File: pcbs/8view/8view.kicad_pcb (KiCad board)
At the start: 4 copper layers, 23.6 x 35.6 mm, 40 parts, among them J1 Conn_01x10_Female, J2 Conn_01x10_Female, J3 Conn_01x06_Female, J4 Conn_01x06_Female, U1 ATtiny828-A, U2 HDSP-A151, U3 HDSP-A151

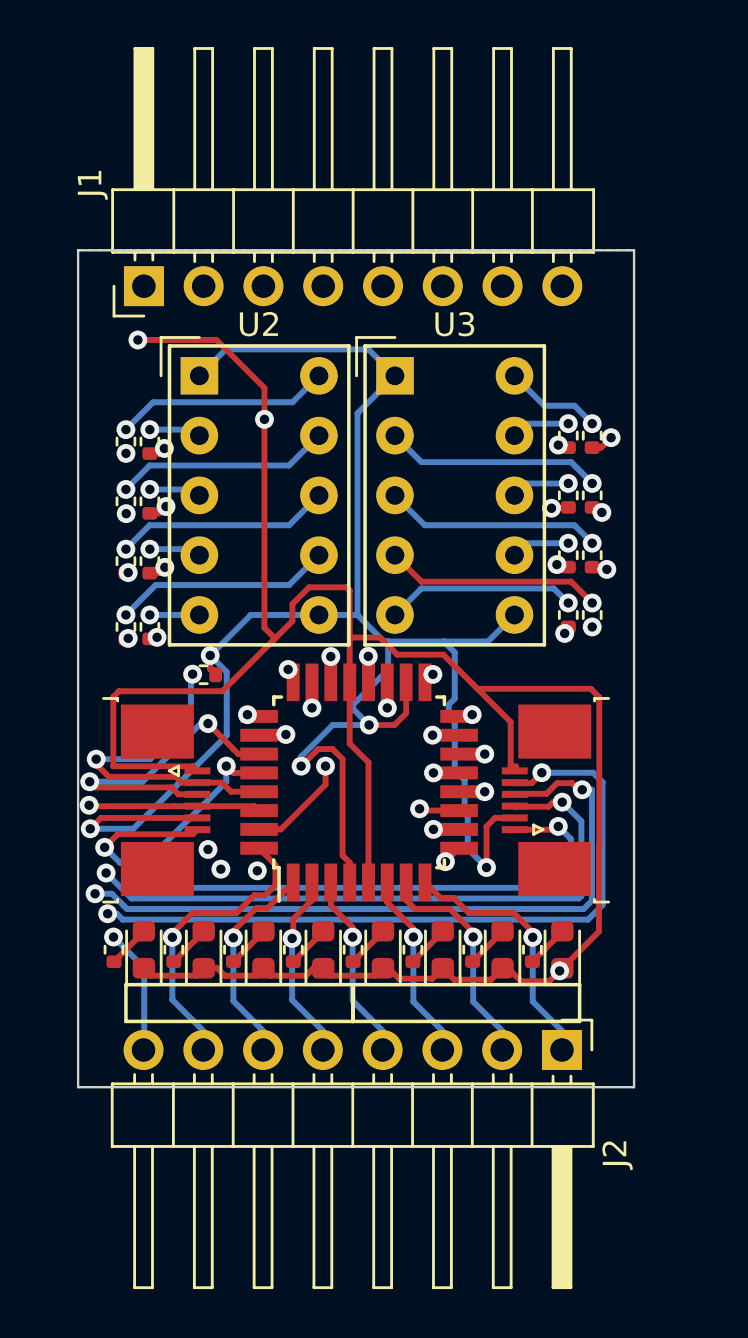
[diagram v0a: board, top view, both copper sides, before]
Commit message: v1 8view borads
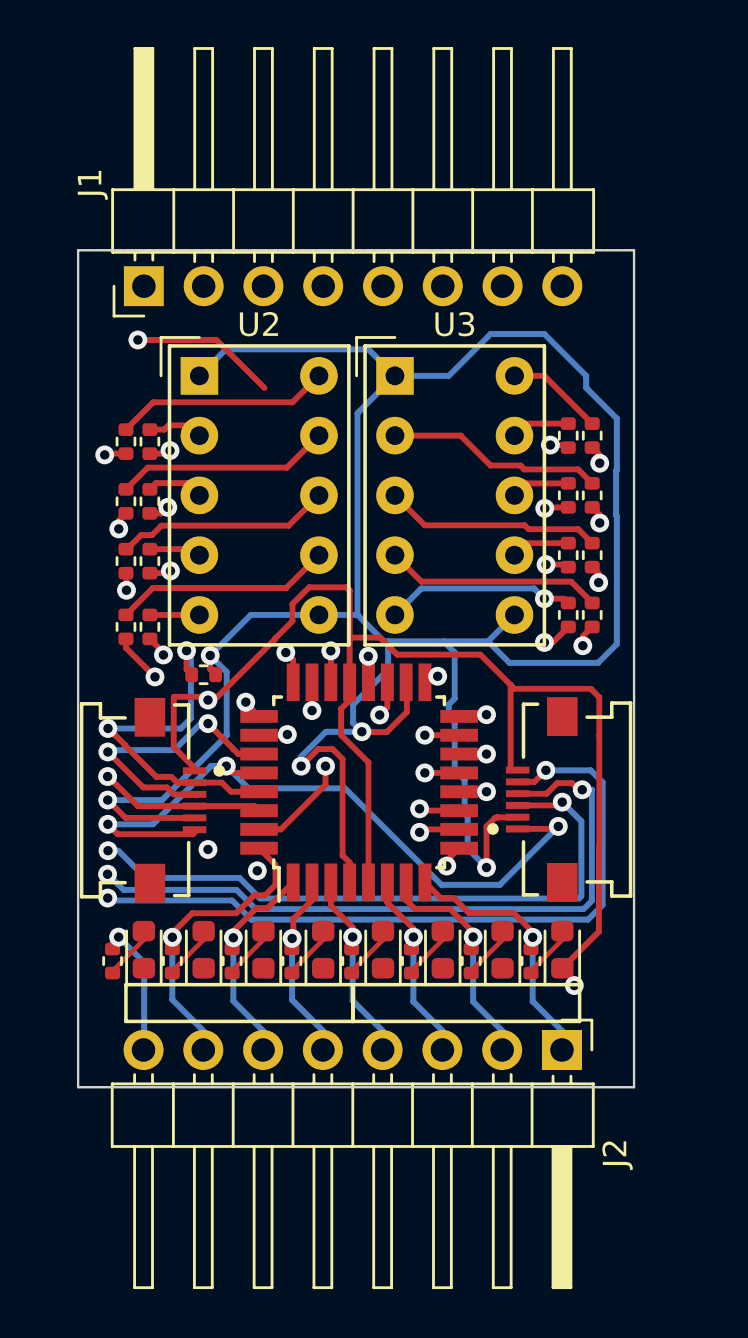
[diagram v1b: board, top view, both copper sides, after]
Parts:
- J3, J4: footprint Connector_FFC-FPC:TE_0-1734839-6_1x06-1MP_P0.5mm_Horizontal -> ffc:Molex-54550-0671-Manufacturer_Recommended
- moved R1 0.49 mm to (137.1, 147.0)
- moved R2 0.49 mm to (139.6, 147.0)
- moved R3 0.49 mm to (142.2, 147.0)
- moved R4 0.49 mm to (144.7, 147.0)
- moved R5 0.49 mm to (147.3, 147.0)
- moved R6 0.49 mm to (149.8, 147.0)
- moved R7 0.49 mm to (152.3, 147.0)
- moved R8 0.49 mm to (154.9, 147.0)
- moved J3 0.28 mm to (155.3, 140.2)
- moved J4 0.28 mm to (139.6, 140.2)
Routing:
- net +5V: track 84.1 -> 110.3 mm
- net GND: track 96.8 -> 89.8 mm
- net /ISP_MISO: track 37.2 -> 30.6 mm
- net /ISP_RST: track 53.1 -> 56.2 mm
- net /D1_I5: track 28.2 -> 26.5 mm
- net /D1_I3: track 24.6 -> 23.3 mm
- net /ISP_SCK: track 38.3 -> 39.5 mm
- net /D1_I7: track 32.4 -> 31.3 mm
- net /D2_I8: track 18.6 -> 19.6 mm
- net /ISP_MOSI: track 50.0 -> 49.1 mm
- net /in2: track 47.8 -> 48.5 mm
- net Net-(D1-Pad2): track 1.82 -> 2.58 mm
- net /in3: track 44.4 -> 45.0 mm
- net /D2_I1: track 33.0 -> 33.6 mm
- net /D2_I7: track 13.2 -> 12.7 mm
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
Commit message: 8view: 10pin skirt, 1.5k leds
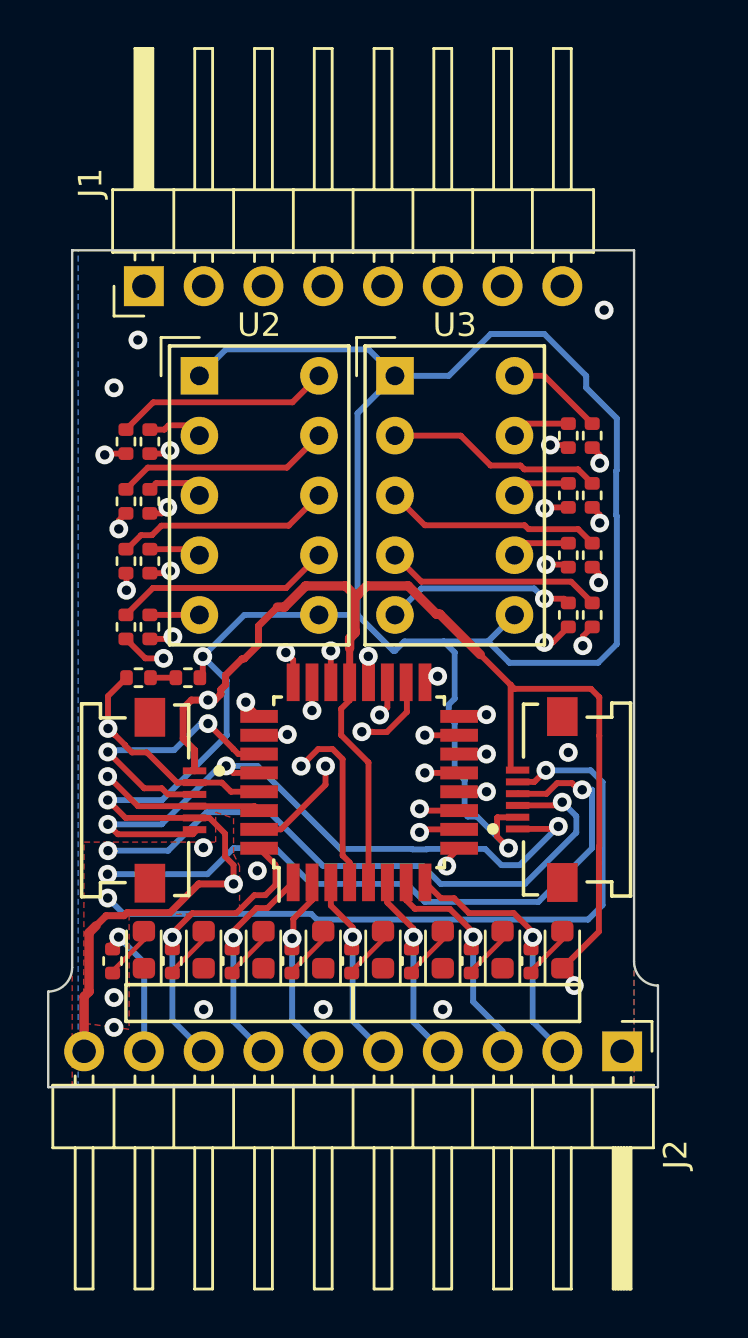
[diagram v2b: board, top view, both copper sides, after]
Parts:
- added R10: 1k5, Resistor_SMD:R_0402_1005Metric, F.Cu at (138.2, 135.0)
- J2: footprint Connector_PinHeader_2.54mm:PinHeader_1x08_P2.54mm_Horizontal -> Connector_PinHeader_2.54mm:PinHeader_1x10_P2.54mm_Horizontal
- R1, R2, R3, R4, R5, R6, R7, R8, R9: value 1000 -> 1k5
- R11: renamed from R10; value 1000 -> 1k
- R12: renamed from R11; value 1000 -> 1k
- R13: renamed from R12; value 1000 -> 1k
- R14: renamed from R13; value 1000 -> 1k
- R15: renamed from R14; value 1000 -> 1k
- R16: renamed from R15; value 1000 -> 1k
- R17: renamed from R16; value 1000 -> 1k
- R18: renamed from R17; value 1000 -> 1k
- R19: renamed from R18; value 1000 -> 1k
- R20: renamed from R19; value 1000 -> 1k
- R21: renamed from R20; value 1000 -> 1k
- R22: renamed from R21; value 1000 -> 1k
- R23: renamed from R22; value 1000 -> 1k
- R24: renamed from R23; value 1000 -> 1k
- R25: renamed from R24; value 1000 -> 1k
- R26: renamed from R25; value 1000 -> 1k
- moved J2 2.56 mm to (158.8, 150.9)
- moved R9 0.68 mm to (140.3, 135.0)
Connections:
- J2 pad 1: /in7 -> GND
- J2 pad 2: /in6 -> /in7
- J2 pad 3: /in5 -> /in6
- J2 pad 4: /in4 -> /in5
- J2 pad 5: /in3 -> /in4
- J2 pad 6: /in2 -> /in3
- J2 pad 7: /in1 -> /in2
- J2 pad 8: /in0 -> /in1
- R9 pad 2: /ISP_RST -> Net-(R9-Pad2)
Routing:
- net GND: track 89.8 -> 76.4 mm, vias 3 -> 7
- net /in0: track 55.6 -> 46.9 mm
- net /in1: track 55.9 -> 47.9 mm
- net +5V: track 110.3 -> 117.9 mm, vias 5 -> 10
- net /ISP_RST: track 56.2 -> 50.9 mm, vias 4 -> 3
- net /in6: track 38.6 -> 42.0 mm
- net /ISP_SCK: track 39.5 -> 37.9 mm
- net /in4: track 42.6 -> 41.2 mm
- net /in5: track 38.8 -> 40.0 mm
- net Net-(R9-Pad2): track 0.00 -> 1.08 mm
- net /ISP_MOSI: track 49.1 -> 48.2 mm
- net /in3: track 45.0 -> 44.1 mm
- net /in2: track 48.5 -> 47.7 mm
- net /in7: track 40.5 -> 41.4 mm
- net /D2_I7: track 12.7 -> 13.4 mm
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- added copper zone on F.Cu, net +5V
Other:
- board size 23.6 x 35.6 mm -> 25.9 x 35.6 mm

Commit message: 8view: testpoints
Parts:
- added TP1: TestPoint, TestPoint:TestPoint_Pad_D1.5mm, B.Cu at (146.9, 141.0)
- added TP2: TestPoint, TestPoint:TestPoint_Pad_D1.5mm, B.Cu at (154.9, 136.8)
- added TP3: TestPoint, TestPoint:TestPoint_Pad_D1.5mm, B.Cu at (142.4, 141.0)
- added TP4: TestPoint, TestPoint:TestPoint_Pad_D1.5mm, B.Cu at (146.9, 143.9)
- added TP5: TestPoint, TestPoint:TestPoint_Pad_D1.5mm, B.Cu at (140.9, 144.8)
- added TP6: TestPoint, TestPoint:TestPoint_Pad_D1.5mm, B.Cu at (157.5, 136.8)
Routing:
- net GND: track 76.4 -> 78.2 mm
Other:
- board text added: "GN"
- board text added: "V+"

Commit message: 8view: caps++
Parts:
- added C1: 1p, Capacitor_SMD:C_0603_1608Metric, F.Cu at (154.4, 134.9)
- added C2: 1p, Capacitor_SMD:C_0603_1608Metric, F.Cu at (140.7, 134.9)
- moved R9 2.71 mm to (137.6, 134.8), turned to 90 degrees
- moved R10 1.71 mm to (136.5, 134.8), turned to -90 degrees
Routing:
- net +5V: track 117.9 -> 88.7 mm
- net GND: track 78.2 -> 63.9 mm
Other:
- board text added: "8view"
- board text added: "BreadV"
- board text added: "v1.1"

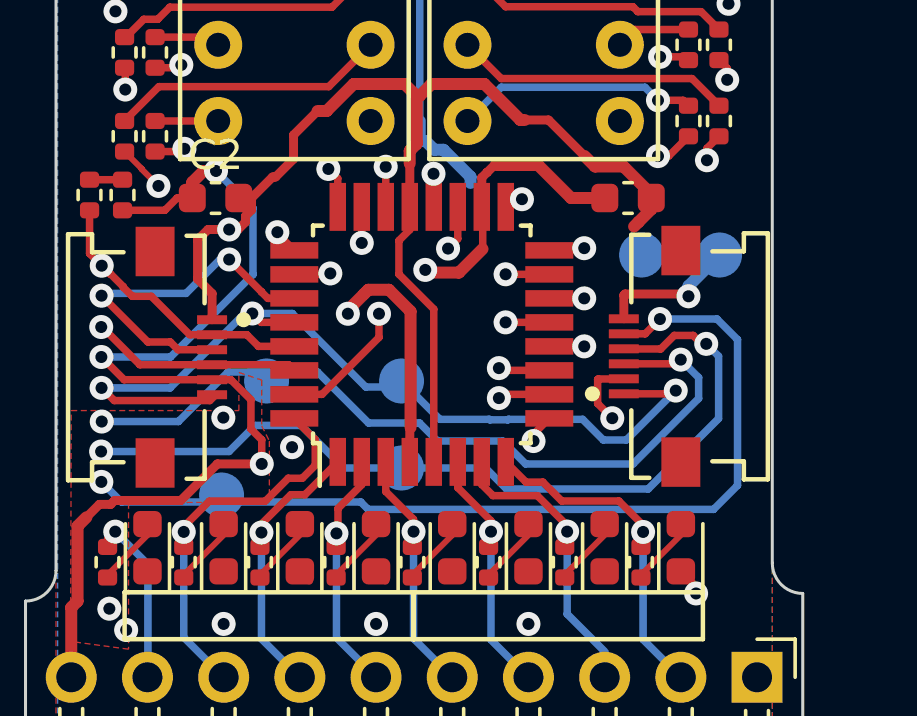
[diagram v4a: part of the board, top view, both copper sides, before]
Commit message: 8view: nicer tp labels
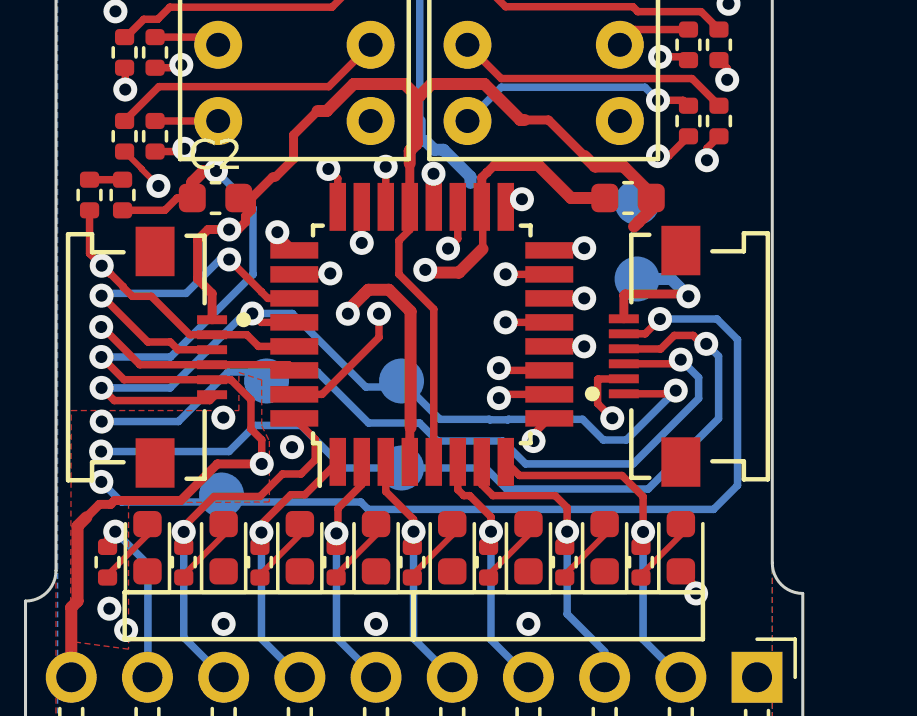
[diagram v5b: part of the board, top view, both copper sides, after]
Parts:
- moved TP6 2.86 mm to (154.8, 137.6)
- moved TP2 1.76 mm to (154.8, 135.1)
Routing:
- net /in7: track 41.4 -> 41.9 mm
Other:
- board text added: "CK"
- board text added: "MI MO"
- board text added: "RS"
- board text added: "VC"
- board text added: "VC GN"
- board text removed: "V+"

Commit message: 8view: v1.1 touches
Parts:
- D1, D2, D3, D4: value LED -> GREEN
- D5, D6, D7, D8: value LED -> RED
- moved R10 0.30 mm to (136.8, 134.8)
- moved R9 0.25 mm to (137.8, 134.8)
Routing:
- net /D1_I8: track 19.6 -> 37.8 mm, vias 2 -> 3
- net /D1_I1: track 33.3 -> 31.9 mm
- net GND: track 63.9 -> 64.6 mm
- net /D1_I6: track 34.2 -> 33.6 mm
